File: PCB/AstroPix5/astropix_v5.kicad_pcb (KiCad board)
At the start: 4 copper layers, 51.3 x 48.9 mm, 37 parts, among them J1 pcie_GECCO, J10 SPI_right, J11 HV, J2 Conn_02x04_Odd_Even, J4 SFOut, J6 HV_in_external, J8 HBOut, J9 SPI_left, U1 AstroPix4_split_powerring

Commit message: Small modifications in schematic and layout finished
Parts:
- removed FID1, FID2: Fiducial, Fiducial:Fiducial_1mm_Mask2mm
- removed H1, H2: MountingHole, MountingHole:MountingHole_3.2mm_M3
- removed H3: bonder, astropix:bonder
- removed J10: SPI_right, Connector_PinHeader_2.54mm:PinHeader_1x06_P2.54mm_Vertical
- removed J11: HV, Connector_PinHeader_2.54mm:PinHeader_1x05_P2.54mm_Vertical
- removed J6: HV_in_external, Connector_Coaxial:SMA_Molex_73251-2200_Horizontal
- removed J9: SPI_left, Connector_PinHeader_2.54mm:PinHeader_1x06_P2.54mm_Vertical
- removed JP1: VDD_JP, Connector_PinHeader_2.54mm:PinHeader_1x03_P2.54mm_Vertical
- removed Logo1: KIT_logo, astropix:logo
- removed Logo2, Logo3: HV_logo, astropix:hv
- removed R10, R13, R14, R17, R18: 22, Resistor_SMD:R_0402_1005Metric
- removed R12: 1k, Resistor_SMD:R_0603_1608Metric
- removed U1: AstroPix4_split_powerring, astropix:AstroPix4
- added C3: 100 nF, Capacitor_SMD:C_0603_1608Metric, F.Cu at (175.4, 115.2)
- added FID3: Fiducial, Fiducial:Fiducial_1mm_Mask2mm, F.Cu at (209.0, 82.2)
- added FID4: Fiducial, Fiducial:Fiducial_1mm_Mask2mm, F.Cu at (203.1, 65.3)
- added H4: MountingHole, MountingHole:MountingHole_3.2mm_M3, F.Cu at (194.8, 80.9)
- added H5: MountingHole, MountingHole:MountingHole_3.2mm_M3, F.Cu at (169.9, 121.4)
- added H6: MountingHole, MountingHole:MountingHole_3.2mm_M3, F.Cu at (168.2, 82.9)
- added H6: bonder, astropix:bonder, F.Cu at (182.0, 98.2)
- added J12: Measures_Analog, Connector_PinHeader_2.54mm:PinHeader_1x04_P2.54mm_Vertical, F.Cu at (208.8, 108.5)
- added J13: pcie_GECCO, Connector_PCBEdge:BUS_PCIexpress_x16, F.Cu at (156.0, 130.5)
- added J14: Bias, Connector_PinHeader_2.54mm:PinHeader_1x12_P2.54mm_Horizontal, F.Cu at (170.8, 61.2)
- added J3: SPI_left, Connector_PinHeader_2.54mm:PinHeader_1x06_P2.54mm_Vertical, F.Cu at (158.2, 89.1)
- added J5: HBOut, Connector_Coaxial:SMA_Molex_73251-2200_Horizontal, F.Cu at (160.5, 118.2)
- added J7: HV_in_external, Connector_Coaxial:SMA_Molex_73251-2200_Horizontal, F.Cu at (160.5, 77.5)
- added JP3: Jumper_3_Bridged12, Connector_PinHeader_2.54mm:PinHeader_1x03_P2.54mm_Vertical, F.Cu at (188.8, 74.9)
- added JP4: Jumper_2_Bridged, Connector_PinHeader_2.54mm:PinHeader_1x02_P2.54mm_Vertical, F.Cu at (184.0, 74.9)
- added JP5: Jumper_2_Bridged, Connector_PinHeader_2.54mm:PinHeader_1x02_P2.54mm_Vertical, F.Cu at (179.0, 74.9)
- added Logo4: KIT_logo, astropix:logo, F.Cu at (161.1, 63.6)
- added Logo5: HV_logo, astropix:hv, F.Cu at (168.3, 77.6)
- added R3: 2k2, Resistor_SMD:R_0603_1608Metric, F.Cu at (165.7, 119.0)
- added R4: 10k, Resistor_SMD:R_0603_1608Metric, F.Cu at (202.1, 106.3)
- added R6: 10k, Resistor_SMD:R_0603_1608Metric, F.Cu at (191.8, 116.8)
- added TP1: TestPoint, TestPoint:TestPoint_Loop_D1.80mm_Drill1.0mm_Beaded, F.Cu at (209.0, 90.0)
- added TP2: TestPoint, TestPoint:TestPoint_Loop_D1.80mm_Drill1.0mm_Beaded, F.Cu at (209.0, 94.0)
- added U2: AstroPix5_split_powerring, astropix:AstroPix5_v2, F.Cu at (175.1, 87.4)
- C10: value 10uF -> .1uF
- C11: value 1nF -> 10uF
- C13: value .1uF -> 10uF
- C14: value 10uF -> 1nF; footprint Capacitor_SMD:C_0603_1608Metric -> Capacitor_SMD:C_1210_3225Metric
- C15: value 10uF -> .1uF; footprint Capacitor_SMD:C_0603_1608Metric -> Capacitor_SMD:C_1210_3225Metric
- C4: value 1nF -> 10uF; footprint Capacitor_SMD:C_1210_3225Metric -> Capacitor_SMD:C_0603_1608Metric
- C6: value .1uF -> 1nF; footprint Capacitor_SMD:C_1210_3225Metric -> Capacitor_SMD:C_0603_1608Metric
- J1: value pcie_GECCO -> HBOut; footprint astropix:pcie_astropix -> Connector_Coaxial:SMA_Molex_73251-2200_Horizontal
- J2: value Conn_02x04_Odd_Even -> Conn_01x05; footprint Connector_PinHeader_2.54mm:PinHeader_2x04_P2.54mm_Vertical -> Connector_PinHeader_2.54mm:PinHeader_1x05_P2.54mm_Vertical
- J4: value SFOut -> HBOut
- J8: value HBOut -> Conn_01x03; footprint Connector_Coaxial:SMA_Molex_73251-2200_Horizontal -> Connector_PinHeader_2.54mm:PinHeader_1x03_P2.54mm_Vertical
- R1: value 2.2k -> 1k
- R2: value 2.2k -> 2k2
- moved C10 84.2 mm to (199.5, 111.2)
- moved C13 83.3 mm to (201.0, 111.2), turned to -90 degrees
- moved C8 79.6 mm to (198.0, 111.2)
- moved J1 79.5 mm to (206.6, 118.2), turned to -90 degrees
- moved J8 68.2 mm to (204.8, 106.0), turned to 180 degrees
- moved C6 63.3 mm to (169.7, 110.2), turned to -90 degrees
- moved R2 62.4 mm to (200.1, 118.7)
- moved C4 55.3 mm to (166.1, 106.0)
- moved J4 53.8 mm to (206.6, 75.0)
- moved C9 52.3 mm to (168.2, 110.2)
- moved C1 48.9 mm to (163.1, 106.0), turned to 90 degrees
- moved C14 48.8 mm to (166.3, 98.4), turned to 0 degrees
- moved C11 48.1 mm to (166.7, 110.2), turned to -90 degrees
- moved C15 47.7 mm to (166.3, 95.2), turned to 0 degrees
- moved C2 47.3 mm to (164.6, 106.0), turned to 90 degrees
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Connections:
- C1 pad 1: VSSA -> VDD
- C10 pad 1: VDD -> VDDA
- C11 pad 1: VDDA -> VSSA
- C14 pad 1: VDDA -> GND
- C14 pad 2: GND -> suba
- C15 pad 1: VSSA -> GND
- C15 pad 2: GND -> suba
- C2 pad 1: VSSA -> VDD
- C4 pad 1: GND -> VDD
- C4 pad 2: suba -> GND
- C6 pad 1: GND -> VSSA
- C6 pad 2: suba -> GND
- C8 pad 1: VDD -> VDDA
- C9 pad 1: VDD -> VSSA
- J2 pad 1: /Vtemp1 -> Net-(J2-Pin_1)
- J2 pad 2: /pload -> Net-(J2-Pin_2)
- J2 pad 3: /Vtemp2 -> Net-(J2-Pin_3)
- J2 pad 4: /VPBias -> Net-(J2-Pin_4)
- J2 pad 5: /vdac_test -> Net-(J2-Pin_5)
- J8 pad 1: Net-(J8-In) -> /interrupt
- J8 pad 2: GND -> unconnected-(J8-Pin_2-Pad2)
- R1 pad 1: Net-(J8-In) -> /HV_in_ext
- R1 pad 2: GND -> suba
- R2 pad 1: Net-(J4-In) -> Net-(J1-In)
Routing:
- net GND: track 17.5 -> 169.3 mm, vias 50 -> 17
- net /blpix: track 0.00 -> 102.0 mm, vias 0 -> 4
- net /ThPix: track 0.00 -> 92.4 mm, vias 0 -> 4
- net /VCasc2!: track 0.00 -> 88.2 mm, vias 0 -> 4
- net Net-(J14-Pin_1): track 0.00 -> 81.9 mm, vias 0 -> 2
- net Net-(J14-Pin_3): track 0.00 -> 80.5 mm, vias 0 -> 2
- net Net-(J14-Pin_4): track 0.00 -> 77.0 mm, vias 0 -> 2
- net Net-(J14-Pin_10): track 0.00 -> 63.9 mm, vias 0 -> 2
- net /spi_left_csn: track 62.4 -> 0.00 mm, vias 1 -> 0
- net /spi_left_clk: track 62.0 -> 0.00 mm, vias 1 -> 0
- net /spi_right_miso1: track 61.8 -> 0.00 mm, vias 1 -> 0
- net Net-(J14-Pin_5): track 0.00 -> 60.8 mm, vias 0 -> 1
- net Net-(J14-Pin_12): track 0.00 -> 60.7 mm, vias 0 -> 2
- net /spi_right_miso0: track 59.9 -> 0.00 mm, vias 1 -> 0
- net /spi_right_csn: track 59.9 -> 0.00 mm, vias 1 -> 0
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- added copper zone on In2.Cu, net VDD
- added copper zone on In2.Cu, net VDDA
- added copper zone on In2.Cu, net VSSA
- removed copper zone on B.Cu, net GND
- removed copper zone on F.Cu, net GND
- removed copper zone on In2.Cu, net GND
- removed copper zone on F.Cu, net VSSA
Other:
- board size 51.3 x 48.9 mm -> 56.4 x 65.5 mm
- board text added: "ADL I.Munnich March 2026"
- board text added: "AstroPix5"
- board text removed: "ADL"
- board text removed: "AstroPix4"
- board text removed: "N. Striebig Sep 2023"

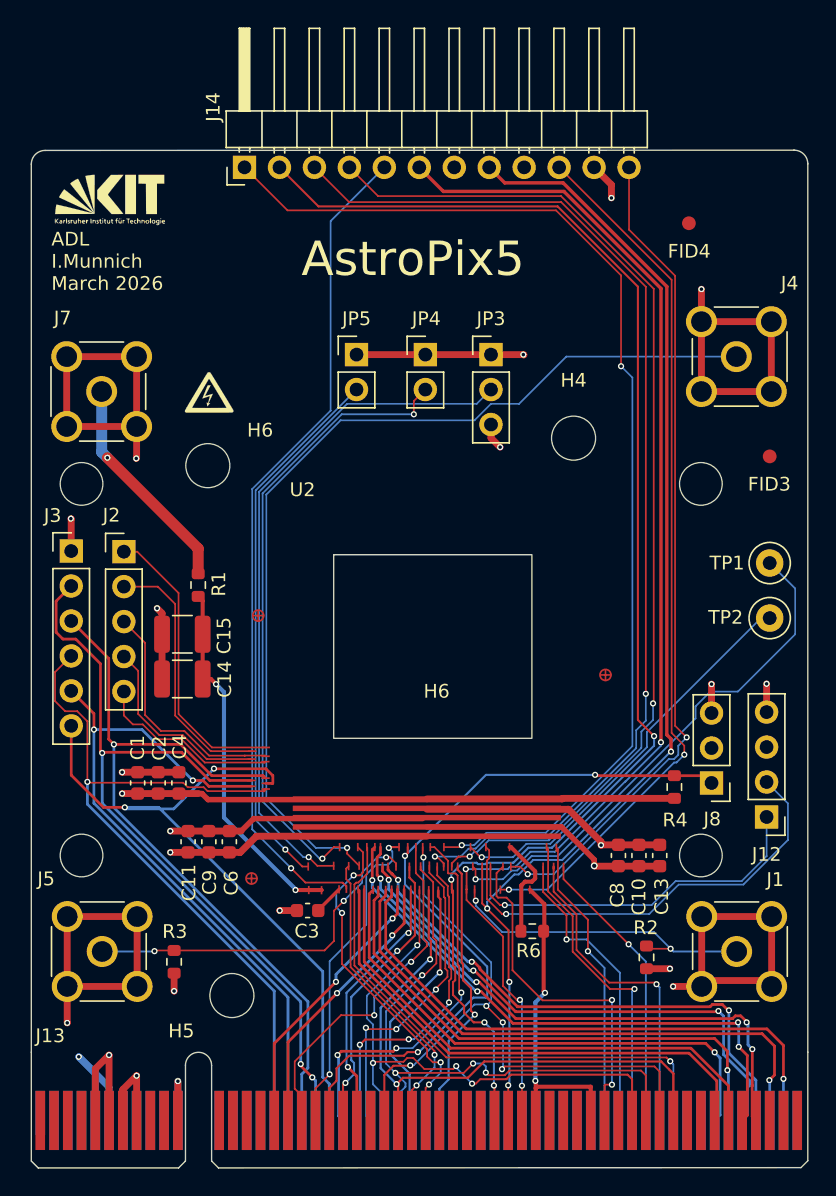
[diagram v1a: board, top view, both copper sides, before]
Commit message: Layout change schematic pcie change
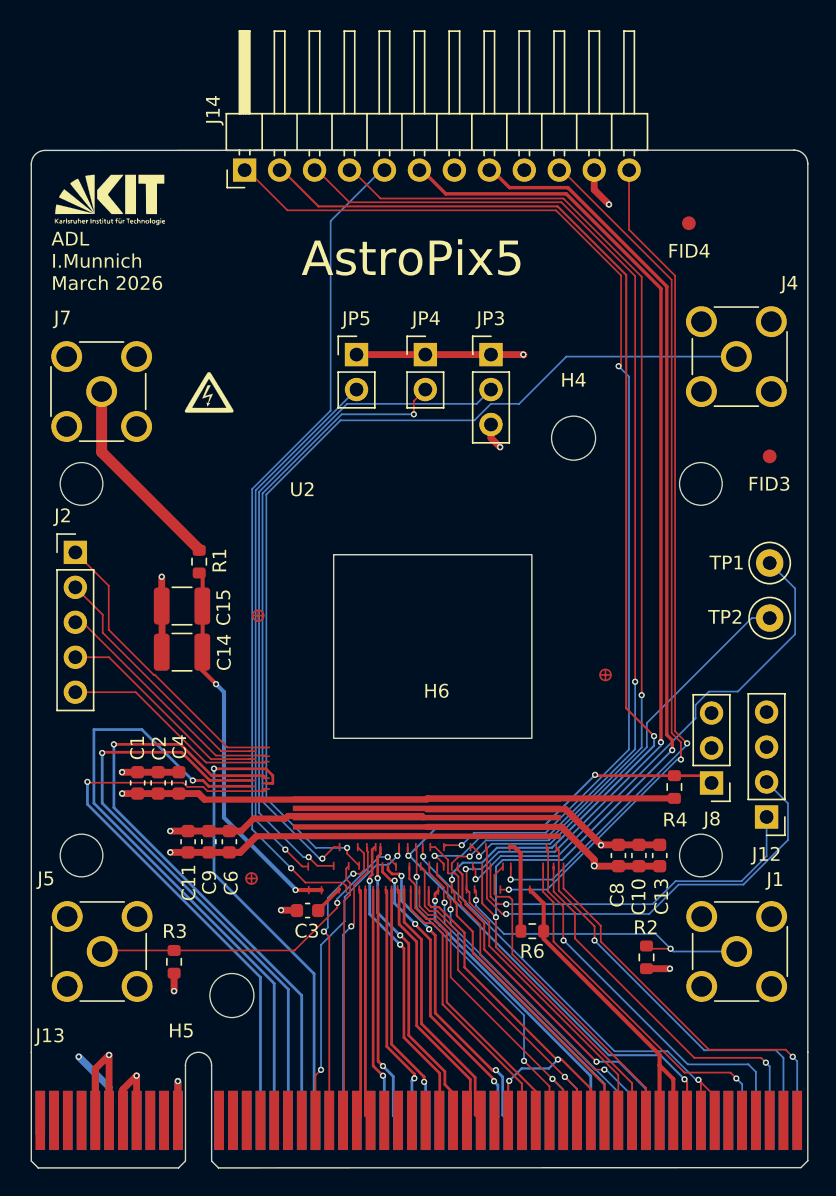
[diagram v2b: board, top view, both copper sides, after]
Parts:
- removed the H6 at (168.2, 82.9)
- removed J3: SPI_left, Connector_PinHeader_2.54mm:PinHeader_1x06_P2.54mm_Vertical
- moved J2 3.53 mm to (158.6, 89.2)
- moved C15 2.05 mm to (166.3, 93.1)
- moved C14 1.95 mm to (166.3, 96.5)
- moved R1 1.70 mm to (167.6, 89.9)
- moved J14 0.20 mm to (170.8, 61.5)
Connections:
- J13 pad A15: unconnected-(J13-C1_6-PadA15) -> /SPI_left_CSN
- J13 pad A16: /SPI_left_CSN -> /SPI_left_CLK
- J13 pad A17: /SPI_left_CLK -> /SPI_left_MISO0
- J13 pad A19: /SPI_left_MISO0 -> /SPI_left_MOSI
- J13 pad A20: /SPI_left_MOSI -> unconnected-(J13-FMC_LA19_P-PadA20)
- J13 pad A21: /SR_ldtdac -> /Enable_SPI_diff
- J13 pad A22: /SR_sout -> unconnected-(J13-FMC_LA17_CC_P-PadA22)
- J13 pad A23: /SR_rb -> unconnected-(J13-FMC_LA17_CC_N-PadA23)
- J13 pad A24: /SR_ck1 -> /SPI_MOSI_P
- J13 pad A25: /SR_ck2 -> /SPI_MOSI_N
- J13 pad A26: /SR_ldpatgen -> /SPI_CSN_P
- J13 pad A27: unconnected-(J13-C2_6-PadA27) -> /SPI_CSN_N
- J13 pad A28: /Inj -> unconnected-(J13-C3_1-PadA28)
- J13 pad A32: unconnected-(J13-C4_1-PadA32) -> /SPI_CLK_P
- J13 pad A33: unconnected-(J13-C4_2-PadA33) -> /SPI_CLK_N
- J13 pad A37: unconnected-(J13-C5_2-PadA37) -> /SR_ck1
- J13 pad A38: unconnected-(J13-C5_5-PadA38) -> /SR_ck2
- J13 pad A39: unconnected-(J13-C5_6-PadA39) -> /SR_ldpatgen
- J13 pad A40: /SPI_right_CLK -> /SR_rb
- J13 pad A41: /SPI_right_MISO1 -> /SR_sout
- J13 pad A42: /SPI_right_MISO0 -> /SR_ldtdac
- J13 pad A43: /SPI_right_CSN -> /Inj
- J13 pad A44: /SPI_right_MOSI -> unconnected-(J13-FMC_LA11_P-PadA44)
- J13 pad A45: /Enable_SPI_diff -> unconnected-(J13-FMC_LA11_N-PadA45)
- J13 pad A48: /SPI_MOSI_P -> unconnected-(J13-FMC_LA07_P-PadA48)
- J13 pad A49: /SPI_MOSI_N -> unconnected-(J13-FMC_LA07_N-PadA49)
- J13 pad A50: /SPI_CLK_P -> /SPI_right_MISO1
- J13 pad A51: /SPI_CLK_N -> /SPI_right_MISO0
- J13 pad A52: /SPI_CSN_P -> /SPI_right_MOSI
- J13 pad A53: /SPI_CSN_N -> /SPI_right_CLK
- J13 pad A54: unconnected-(J13-FMC_LA03_P-PadA54) -> /SPI_right_CSN
- J13 pad B16: /Clk20_Ext_P -> unconnected-(J13-FMC_LA24_P-PadB16)
- J13 pad B17: /Clk20_Ext_N -> unconnected-(J13-FMC_LA24_N-PadB17)
- J13 pad B18: /hold -> unconnected-(J13-FMC_LA22_P-PadB18)
- J13 pad B20: /interrupt -> /SR_out_CK1
- J13 pad B21: /res_n -> /SR_out_0D
- J13 pad B22: /syncres -> /SPI_MISO1_P
- J13 pad B23: unconnected-(J13-FMC_LA18_CC_N-PadB23) -> /SPI_MISO1_N
- J13 pad B24: /SR_load -> unconnected-(J13-C2_4-PadB24)
- J13 pad B25: /SR_sin -> unconnected-(J13-C2_3-PadB25)
- J13 pad B26: /SR_out_0D -> unconnected-(J13-C2_8-PadB26)
- J13 pad B27: /SR_out_CK1 -> unconnected-(J13-C2_7-PadB27)
- J13 pad B28: unconnected-(J13-C3_4-PadB28) -> /SPI_MISO0_P
- J13 pad B29: unconnected-(J13-C3_3-PadB29) -> /SPI_MISO0_N
- J13 pad B30: unconnected-(J13-C3_8-PadB30) -> /Clk20_Ext_P
- J13 pad B31: unconnected-(J13-C3_7-PadB31) -> /Clk20_Ext_N
- J13 pad B32: /blpix -> unconnected-(J13-C4_4-PadB32)
- J13 pad B33: /VCasc2! -> /SR_sin
- J13 pad B34: /ThPix -> /syncres
- J13 pad B35: /vminuspix -> /res_n
- J13 pad B36: unconnected-(J13-C5_4-PadB36) -> /hold
- J13 pad B37: unconnected-(J13-C5_3-PadB37) -> /SR_ck1
- J13 pad B38: unconnected-(J13-C5_8-PadB38) -> /SR_ck2
- J13 pad B39: /vminuspix -> /SR_sin
- J13 pad B40: /DigInj -> /blpix
- J13 pad B41: unconnected-(J13-FMC_LA16_N-PadB41) -> /ThPix
- J13 pad B42: /SR_ck1 -> /VCasc2!
- J13 pad B43: /SR_ck2 -> /DigInj
- J13 pad B44: /SR_load -> /vminuspix
- J13 pad B45: /SR_sin -> /vminuspix
- J13 pad B46: unconnected-(J13-FMC_LA10_P-PadB46) -> /interrupt
- J13 pad B47: unconnected-(J13-FMC_LA10_N-PadB47) -> /SR_load
- J13 pad B48: /SPI_MISO1_P -> /SR_load
- J13 pad B49: /SPI_MISO1_N -> unconnected-(J13-FMC_LA08_N-PadB49)
- J13 pad B50: /SPI_MISO0_P -> unconnected-(J13-FMC_LA06_P-PadB50)
- J13 pad B51: /SPI_MISO0_N -> unconnected-(J13-FMC_LA06_N-PadB51)
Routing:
- net GND: track 169.3 -> 72.1 mm, vias 17 -> 10
- net /SPI_CSN_P: track 41.7 -> 17.7 mm
- net /SPI_CSN_N: track 41.7 -> 17.8 mm
- net /SPI_MOSI_P: track 38.3 -> 17.1 mm
- net /SPI_MOSI_N: track 38.4 -> 17.4 mm
- net /SPI_MISO1_N: track 38.0 -> 16.9 mm
- net /SPI_MISO1_P: track 37.9 -> 16.9 mm
- net /SPI_MISO0_N: track 41.5 -> 22.2 mm, vias 4 -> 2
- net /SPI_MISO0_P: track 41.3 -> 22.1 mm, vias 4 -> 2
- net /Enable_SPI_diff: track 39.3 -> 20.7 mm
- net /SPI_left_MOSI: track 52.1 -> 34.2 mm, vias 2 -> 1
- net /SR_ck1: track 42.3 -> 24.7 mm, vias 4 -> 1
- net /SR_ck2: track 44.0 -> 27.0 mm, vias 4 -> 1
- net /SPI_CLK_P: track 38.6 -> 22.2 mm
- net /SPI_CLK_N: track 38.8 -> 22.5 mm
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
